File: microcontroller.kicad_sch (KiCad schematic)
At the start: 21 parts, among them J1 SWD, SW1 RESET, U1 STM32F103C8Tx, Y1 8MHz

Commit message: some stuff
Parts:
- renumbered C8 to C10, C9 to C11, C10 to C12, C11 to C13, C12 to C14, C13 to C15, C14 to C16, C15 to C8, C16 to C9, R9 to R10, R10 to R9

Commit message: i2c
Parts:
- added R140, R141, R142, R143: 4.7K, symbol Device:R
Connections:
- net +3.3V: now also R140.1, R141.2, R142.2, R143.1
- net I2C_MASTER_SCL: now reaches U1.21 (PB10)
- net I2C_MASTER_SCL: now also R143.2
- net I2C_MASTER_SDA: now reaches U1.22 (PB11)
- net I2C_MASTER_SDA: now also R142.1
- net I2C_SLAVE_SCL: now reaches U1.42 (PB6)
- net I2C_SLAVE_SCL: now also R140.2
- net I2C_SLAVE_SDA: now reaches U1.43 (PB7)
- net I2C_SLAVE_SDA: now also R141.1
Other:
- moved on the sheet: JP1, JP2, R10, R8

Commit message: wip
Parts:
- removed JP1: BOOT0, symbol Jumper:SolderJumper_3_Open
- removed JP2: BOOT1, symbol Jumper:SolderJumper_3_Open
- added J3: BOOT1, symbol Connector:Conn_01x03_Pin
- added J4: BOOT0, symbol Connector:Conn_01x03_Pin
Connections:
- net +3.3V: now also J3.1 (Pin_1), J4.3 (Pin_3)
- net GND: now also J3.3 (Pin_3), J4.1 (Pin_1)
- net at R10.1: now also J3.2 (Pin_2)
- net at R8.2: now also J4.2 (Pin_2)
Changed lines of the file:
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@@
 	(wire
 		(pts
+			(xy 74.93 88.9) (xy 74.93 91.44)
+		)
+		(stroke
+			(width 0)
+			(type default)
+		)
+	)
+	(wire
+		(pts
 			(xy 74.93 116.84) (xy 128.27 116.84)
 		)
@@
 	(wire
 		(pts
+			(xy 74.93 96.52) (xy 74.93 99.06)
+		)
+		(stroke
+			(width 0)
+			(type default)
+		)
+	)
+	(wire
+		(pts
 			(xy 146.05 55.88) (xy 148.59 55.88)
 		)
@@
 	(wire
 		(pts
+			(xy 55.88 88.9) (xy 55.88 91.44)
+		)
+		(stroke
+			(width 0)
+			(type default)
+		)
+	)
+	(wire
+		(pts
 			(xy 205.74 52.07) (xy 217.17 52.07)
 		)
@@
 	(wire
 		(pts
+			(xy 52.07 93.98) (xy 55.88 93.98)
+		)
+		(stroke
+			(width 0)
+			(type default)
+		)
+	)
+	(wire
+		(pts
 			(xy 74.93 115.57) (xy 74.93 116.84)
 		)
@@
 	(wire
 		(pts
+			(xy 74.93 93.98) (xy 78.74 93.98)
+		)
+		(stroke
+			(width 0)
+			(type default)
+		)
+	)
+	(wire
+		(pts
 			(xy 80.01 114.3) (xy 128.27 114.3)
 		)
@@
 	(wire
 		(pts
+			(xy 55.88 96.52) (xy 55.88 99.06)
+		)
+		(stroke
+			(width 0)
+			(type default)
+		)
+	)
+	(wire
+		(pts
 			(xy 106.68 105.41) (xy 106.68 106.68)
 		)
@@
 	)
 	(symbol
+		(lib_id "Connector:Conn_01x03_Pin")
+		(at 69.85 93.98 0)
+		(unit 1)
+		(exclude_from_sim no)
+		(in_bom yes)
+		(on_board yes)
+		(dnp no)
+		(property "Reference" "J3"
+			(at 73.406 84.582 0)
+			(effects
+				(font
+					(size 1.27 1.27)
+				)
+			)
+		)
+		(property "Value" "BOOT1"
+			(at 73.66 86.868 0)
+			(effects
+				(font
+					(size 1.27 1.27)
+				)
+			)
+		)
+		(property "Footprint" ""
+			(at 69.85 93.98 0)
+			(effects
+				(font
+					(size 1.27 1.27)
+				)
+				(hide yes)
+			)
+		)
+		(property "Datasheet" "~"
+			(at 69.85 93.98 0)
+			(effects
+				(font
+					(size 1.27 1.27)
+				)
+				(hide yes)
+			)
+		)
+		(property "Description" "Generic connector, single row, 01x03, script generated"
+			(at 69.85 93.98 0)
+			(effects
+				(font
+					(size 1.27 1.27)
+				)
+				(hide yes)
+			)
+		)
+		(pin "2"
+		)
+		(pin "3"
+		)
+		(pin "1"
+		)
+		(instances
+			(project "femta-control"
+				(path "/838bf11c-36b7-41d7-9462-fe98a188d617/19a6893b-6e4a-4325-88c3-1ed1bee3cf29"
+					(reference "J3")
+					(unit 1)
+				)
+			)
+		)
+	)
+	(symbol
 		(lib_id "power:GND")
 		(at 123.19 52.07 0)
@@
 	)
 	(symbol
+		(lib_id "Connector:Conn_01x03_Pin")
+		(at 60.96 93.98 180)
+		(unit 1)
+		(exclude_from_sim no)
+		(in_bom yes)
+		(on_board yes)
+		(dnp no)
+		(property "Reference" "J4"
+			(at 57.404 103.378 0)
+			(effects
+				(font
+					(size 1.27 1.27)
+				)
+			)
+		)
+		(property "Value" "BOOT0"
+			(at 57.15 101.092 0)
+			(effects
+				(font
+					(size 1.27 1.27)
+				)
+			)
+		)
+		(property "Footprint" ""
+			(at 60.96 93.98 0)
+			(effects
+				(font
+					(size 1.27 1.27)
+				)
+				(hide yes)
+			)
+		)
+		(property "Datasheet" "~"
+			(at 60.96 93.98 0)
+			(effects
+				(font
+					(size 1.27 1.27)
+				)
+				(hide yes)
+			)
+		)
+		(property "Description" "Generic connector, single row, 01x03, script generated"
+			(at 60.96 93.98 0)
+			(effects
+				(font
+					(size 1.27 1.27)
+				)
+				(hide yes)
+			)
+		)
+		(pin "2"
+		)
+		(pin "3"
+		)
+		(pin "1"
+		)
+		(instances
+			(project "femta-control"
+				(path "/838bf11c-36b7-41d7-9462-fe98a188d617/19a6893b-6e4a-4325-88c3-1ed1bee3cf29"
+					(reference "J4")
+					(unit 1)
+				)
+			)
+		)
+	)
+	(symbol
 		(lib_id "Device:C")
 		(at 167.64 48.26 0)
@@
 	)
 	(symbol
-		(lib_id "Jumper:SolderJumper_3_Open")
-		(at 55.88 93.98 270)
-		(mirror x)
-		(unit 1)
-		(exclude_from_sim no)
-		(in_bom yes)
-		(on_board yes)
-		(dnp no)
-		(fields_autoplaced yes)
-		(property "Reference" "JP1"
-			(at 58.42 92.7099 90)
-			(effects
-				(font
-					(size 1.27 1.27)
-				)
-				(justify left)
-			)
-		)
-		(property "Value" "BOOT0"
-			(at 58.42 95.2499 90)
-			(effects
-				(font
-					(size 1.27 1.27)
-				)
-				(justify left)
-			)
-		)
-		(property "Footprint" ""
-			(at 55.88 93.98 0)
-			(effects
-				(font
-					(size 1.27 1.27)
-				)
-				(hide yes)
-			)
-		)
-		(property "Datasheet" "~"
-			(at 55.88 93.98 0)
-			(effects
-				(font
-					(size 1.27 1.27)
-				)
-				(hide yes)
-			)
-		)
-		(property "Description" "Solder Jumper, 3-pole, open"
-			(at 55.88 93.98 0)
-			(effects
-				(font
-					(size 1.27 1.27)
-				)
-				(hide yes)
-			)
-		)
-		(pin "2"
-		)
-		(pin "1"
-		)
-		(pin "3"
-		)
-		(instances
-			(project "femta-control"
-				(path "/838bf11c-36b7-41d7-9462-fe98a188d617/19a6893b-6e4a-4325-88c3-1ed1bee3cf29"
-					(reference "JP1")
-					(unit 1)
-				)
-			)
-		)
-	)
-	(symbol
 		(lib_id "power:+3.3V")
 		(at 77.47 52.07 0)
@@
 					(unit 1)
 				)
-			)
-		)
-	)
-	(symbol
-		(lib_id "Jumper:SolderJumper_3_Open")
-		(at 74.93 93.98 90)
-		(unit 1)
-		(exclude_from_sim no)
-		(in_bom yes)
-		(on_board yes)
-		(dnp no)
-		(fields_autoplaced yes)
-		(property "Reference" "JP2"
-			(at 72.39 92.7099 90)
-			(effects
-				(font
-					(size 1.27 1.27)
-				)
-				(justify left)
-			)
-		)
-		(property "Value" "BOOT1"
-			(at 72.39 95.2499 90)
-			(effects
-				(font
-					(size 1.27 1.27)
-				)
-				(justify left)
-			)
-		)
-		(property "Footprint" ""
-			(at 74.93 93.98 0)
-			(effects
-				(font
-					(size 1.27 1.27)
-				)
-				(hide yes)
-			)
-		)
-		(property "Datasheet" "~"
-			(at 74.93 93.98 0)
-			(effects
-				(font
-					(size 1.27 1.27)
-				)
-				(hide yes)
-			)
-		)
-		(property "Description" "Solder Jumper, 3-pole, open"
-			(at 74.93 93.98 0)
-			(effects
-				(font
-					(size 1.27 1.27)
-				)
-				(hide yes)
-			)
-		)
-		(pin "2"
-		)
-		(pin "1"
-		)
-		(pin "3"
-		)
-		(instances
-			(project "femta-control"
-				(path "/838bf11c-36b7-41d7-9462-fe98a188d617/19a6893b-6e4a-4325-88c3-1ed1bee3cf29"
-					(reference "JP2")
-					(unit 1)
-				)

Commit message: microcontroller work
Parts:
- added C116: 0.1uF, symbol Device:C
- added JP1: WDT_EN, symbol Jumper:SolderJumper_2_Open
- added R269: 10K, symbol Device:R
- added U62: MAX6369, Package_TO_SOT_SMD:SOT-23-8, symbol Power_Supervisor:MAX6369
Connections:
- net +3.3V: now also C116.1, U62.4 (SET0), U62.6 (SET2), U62.8 (VCC)
- net GND: now also C116.2, R269.2, U62.2 (GND), U62.5 (SET1)
- net RST: now also JP1.2 (B)
- new net: JP1.1 (A), U62.7 (~{WDO})
- new net HANDSHAKE: R269.1, U62.1 (WDI)
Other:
- note added: "Watchdog resets every 1 second, 300ms startup delay"
- moved on the sheet: C10, C11, C12, C13, C14, C15, C16, C7, C8, C9, FB1, J1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

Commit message: work
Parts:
- renumbered C116 to C66, C7 to C67, C8 to C68, C9 to C69, C10 to C70, C11 to C71, C12 to C72, C13 to C73, C14 to C74, C15 to C75, C16 to C76, J4 to J2, J1 to J4, R269 to R119, R8 to R120, R142 to R121, R9 to R122, R143 to R123, R10 to R124, R141 to R125, R140 to R126, R11 to R127, U62 to U27, U1 to U28

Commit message: 540 COMPONENTS I AM LOSING MY MINDDDDDD
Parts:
- renumbered C69 to C10, C70 to C11, C71 to C12, C72 to C13, C73 to C14, C74 to C15, C75 to C16, C76 to C17, C66 to C7, C67 to C8, C68 to C9, JP1 to JP2, R119 to R15, R120 to R16, R121 to R17, R122 to R18, R123 to R19, R124 to R20, R125 to R21, R126 to R22, R127 to R23, U27 to U4, U28 to U5

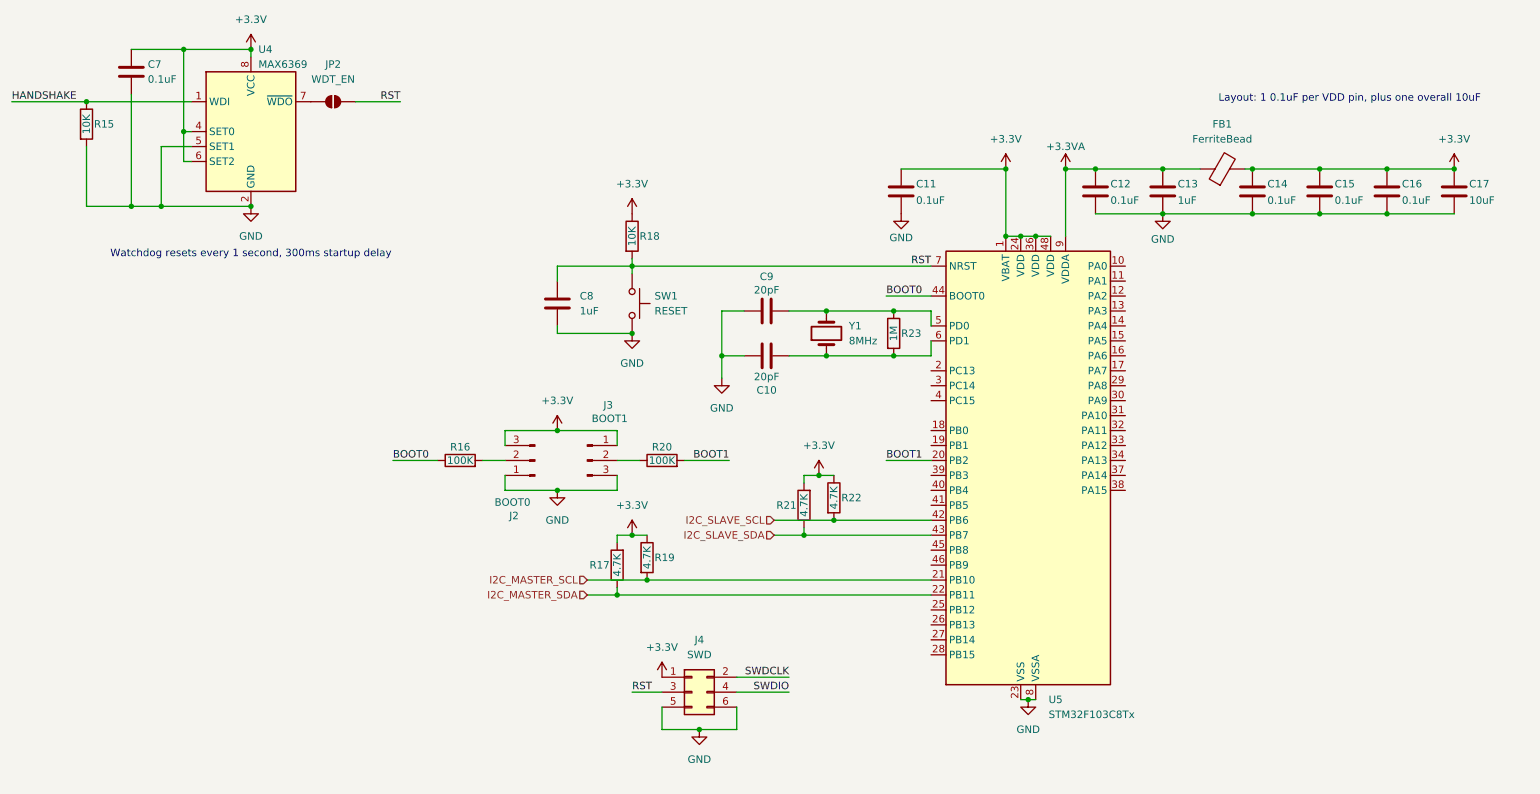
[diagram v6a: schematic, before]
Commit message: page sizes
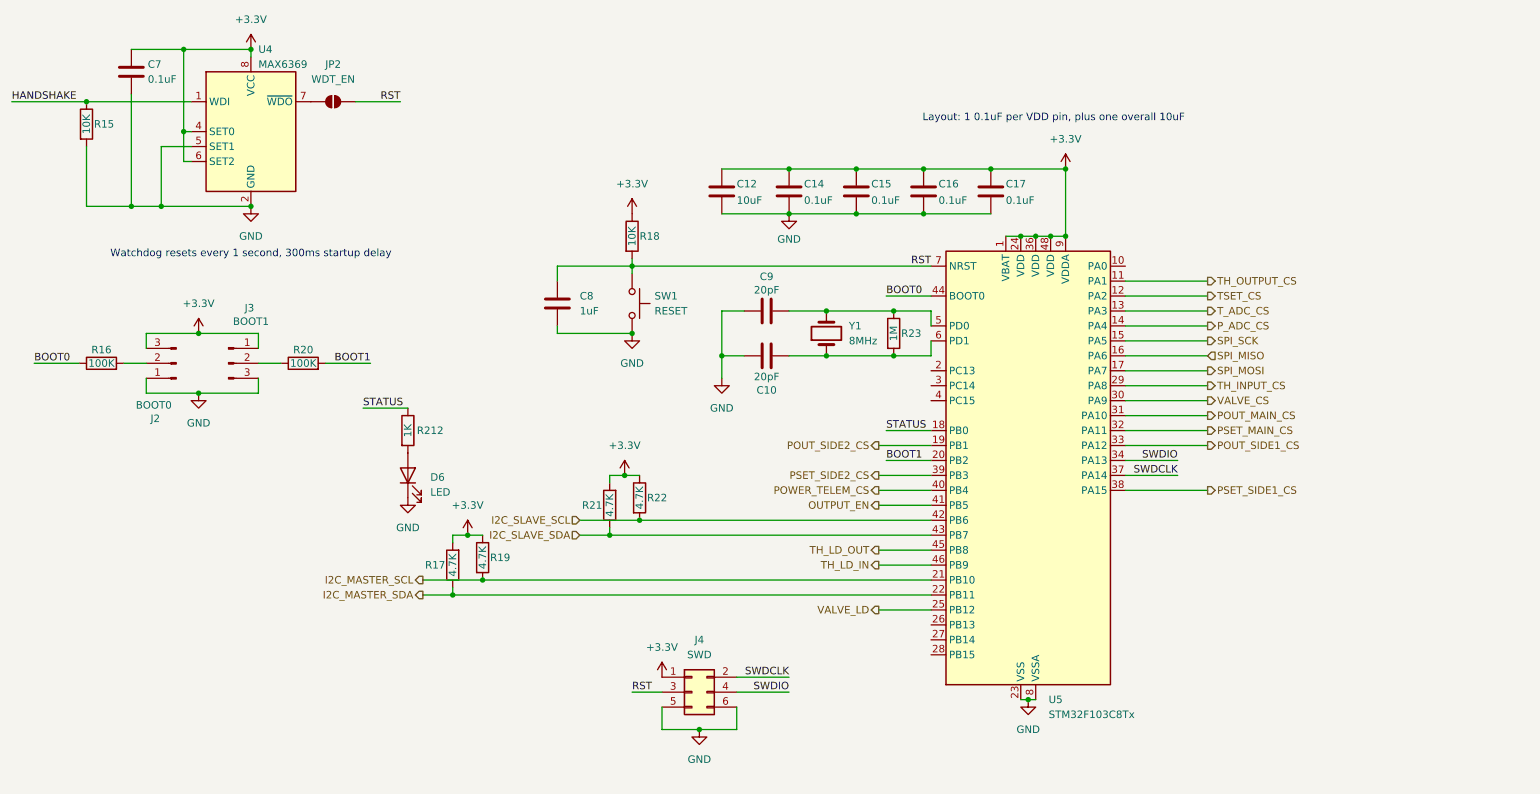
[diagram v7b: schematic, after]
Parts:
- removed C11: 0.1uF, symbol Device:C
- removed C13: 1uF, symbol Device:C
- removed FB1: FerriteBead, symbol Device:FerriteBead
- added D6: LED, symbol Device:LED
- added R212: 1K, symbol Device:R
- C12: value 0.1uF -> 10uF
- C17: value 10uF -> 0.1uF
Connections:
- net +3.3VA is gone; now on net +3.3V: C12.1, U5.9 (VDDA)
- net GND: now also D6.1 (K)
- net SWDCLK: now also U5.37 (PA14)
- net SWDIO: now also U5.34 (PA13)
- net TH_OUTPUT_CS: now reaches U5.11 (PA1)
- net TSET_CS: now reaches U5.12 (PA2)
- net T_ADC_CS: now reaches U5.13 (PA3)
- net P_ADC_CS: now reaches U5.14 (PA4)
- net SPI_SCK: now reaches U5.15 (PA5)
- net SPI_MISO: now reaches U5.16 (PA6)
- net SPI_MOSI: now reaches U5.17 (PA7)
- net STATUS: now reaches U5.18 (PB0)
- net STATUS: now also R212.1
- net POUT_SIDE2_CS: now reaches U5.19 (PB1)
- net VALVE_LD: now reaches U5.25 (PB12)
- net TH_INPUT_CS: now reaches U5.29 (PA8)
- net VALVE_CS: now reaches U5.30 (PA9)
- net POUT_MAIN_CS: now reaches U5.31 (PA10)
- net PSET_MAIN_CS: now reaches U5.32 (PA11)
- net POUT_SIDE1_CS: now reaches U5.33 (PA12)
- net PSET_SIDE1_CS: now reaches U5.38 (PA15)
- net PSET_SIDE2_CS: now reaches U5.39 (PB3)
- net POWER_TELEM_CS: now reaches U5.40 (PB4)
- net OUTPUT_EN: now reaches U5.41 (PB5)
- net TH_LD_OUT: now reaches U5.45 (PB8)
- net TH_LD_IN: now reaches U5.46 (PB9)
- new net: D6.2 (A), R212.2
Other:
- moved on the sheet: C12, C14, C15, C16, C17, J2, J3, R16, R17, R19, R20, R21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

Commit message: schematic finished milestone
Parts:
- renumbered C7 to C10, C8 to C11, C9 to C13, C10 to C14, C14 to C15, C15 to C16, C16 to C17, C17 to C18, D6 to D5, R15 to R23, R16 to R24, R20 to R25, R212 to R26, R17 to R27, R19 to R28, R21 to R29, R18 to R30, R22 to R31, R23 to R32
